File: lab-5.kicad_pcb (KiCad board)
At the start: 4 copper layers, 35 x 70 mm, 48 parts, among them J2 USB_C_Receptacle, J6 Conn_01x24_Pin, SW1 NRST, SW2 BOOT, SW3 USER, U1 LM66100DCK, U2 LM66100DCK, U3 STM32F405RGTx, U5 AP2112K-3.3, Y1 8 MHz

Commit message: add BMP280 via I2C
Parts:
- added C10: 100n, Capacitor_SMD:C_0402_1005Metric, F.Cu at (142.0, 83.7)
- added C9: 100n, Capacitor_SMD:C_0402_1005Metric, F.Cu at (142.0, 80.1)
- added U4: BMP280, Package_LGA:Bosch_LGA-8_2x2.5mm_P0.65mm_ClockwisePinNumbering, F.Cu at (142.8, 81.9)
- added U6: BMI160, Package_LGA:Bosch_LGA-14_3x2.5mm_P0.5mm, F.Cu at (142.7, 87.4)
- added U7: BMM150, Package_CSP:WLCSP-12_1.56x1.56mm_P0.4mm, F.Cu at (143.3, 92.5)
- moved R11 17.1 mm to (148.2, 88.6), turned to -90 degrees
- moved R12 16.5 mm to (148.1, 85.6)
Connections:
- J6 pad 4: /I2C1_SDA -> unconnected-(J6-Pin_4-Pad4)
- J6 pad 5: /I2C1_SCL -> unconnected-(J6-Pin_5-Pad5)
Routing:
- net GND: track 41.1 -> 44.8 mm, vias 35 -> 38
- net +3.3V: track 24.7 -> 28.3 mm, vias 19 -> 22
- net /I2C1_SDA: track 22.1 -> 23.1 mm, vias 0 -> 2
- net /I2C1_SCL: track 22.0 -> 22.7 mm, vias 0 -> 2

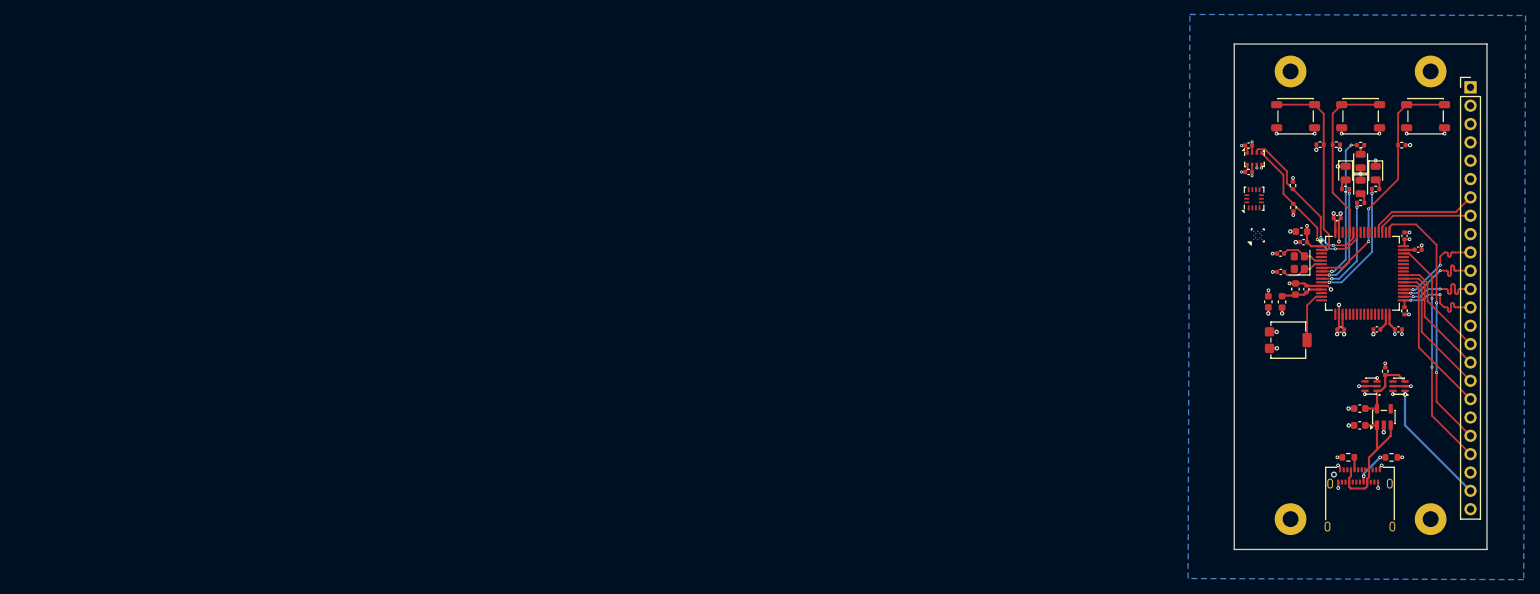
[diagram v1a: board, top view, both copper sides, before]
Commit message: added the BMI160 and logo, full board refactoring
Signed-off-by: Yehor Bilous <bilous801@gmail.com>
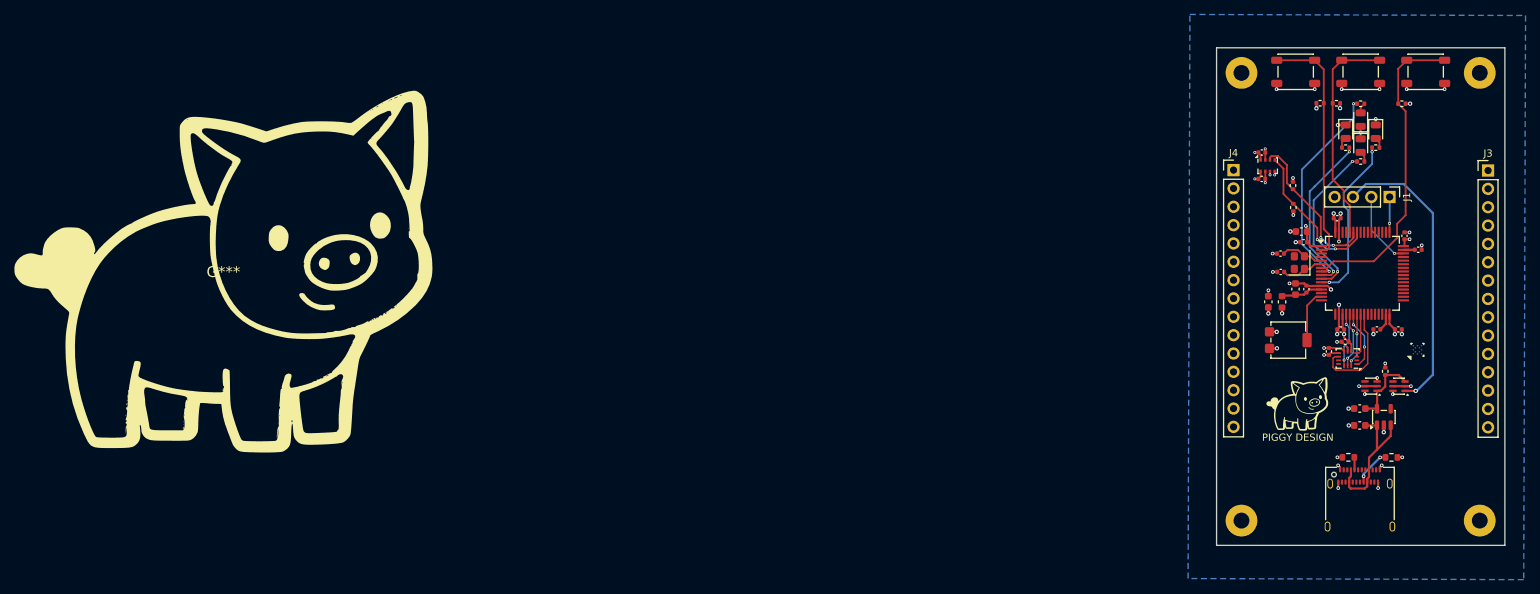
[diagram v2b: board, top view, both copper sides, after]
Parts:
- removed J6: Conn_01x24_Pin, Connector_PinHeader_2.54mm:PinHeader_1x24_P2.54mm_Vertical
- removed R14: 4.7k, Resistor_SMD:R_0402_1005Metric
- added C17: 100n, Capacitor_SMD:C_0402_1005Metric, F.Cu at (153.1, 108.6)
- added C18: 100n, Capacitor_SMD:C_0402_1005Metric, F.Cu at (155.4, 107.2)
- added G***: LOGO, logos:logo, F.Cu at (0.00, 97.6)
- added G***: LOGO, logos:logo10x10, F.Cu at (148.7, 115.8)
- added J1: Conn_01x04_Pin, Connector_PinHeader_2.54mm:PinHeader_1x04_P2.54mm_Vertical, F.Cu at (161.5, 87.2)
- added J3: Conn_01x15_Pin, Connector_PinHeader_2.54mm:PinHeader_1x15_P2.54mm_Vertical, F.Cu at (175.2, 83.5)
- added J4: Conn_01x15_Pin, Connector_PinHeader_2.54mm:PinHeader_1x15_P2.54mm_Vertical, F.Cu at (139.9, 83.5)
- moved U7 27.2 mm to (165.4, 108.3)
- moved U6 25.6 mm to (155.7, 109.6), turned to 180 degrees
- moved H1 6.80 mm to (141.0, 70.0)
- moved H2 6.80 mm to (174.0, 70.0)
- moved H3 6.80 mm to (141.0, 132.0)
- moved H4 6.80 mm to (174.0, 132.0)
- moved SW1 6.15 mm to (166.5, 69.8)
- moved SW2 6.15 mm to (157.5, 69.8)
- moved SW3 6.15 mm to (148.5, 69.8)
- moved D1 5.73 mm to (157.5, 76.5)
- moved D3 5.73 mm to (157.5, 80.1)
- moved R10 5.73 mm to (159.6, 80.3)
- moved R4 5.73 mm to (157.5, 74.3)
- moved R5 5.73 mm to (163.2, 74.3)
- moved R6 5.73 mm to (154.2, 74.2)
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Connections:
- net /USER renamed /USER_BUTTON
- U3 pad 20: unconnected-(U3-PA4-Pad20) -> /SPI1_NSS
- U3 pad 21: unconnected-(U3-PA5-Pad21) -> /SPI1_SCK
- U3 pad 22: unconnected-(U3-PA6-Pad22) -> /SPI1_MISO
- U3 pad 23: unconnected-(U3-PA7-Pad23) -> /SPI1_MOSI
- U3 pad 24: unconnected-(U3-PC4-Pad24) -> /GPIO_EXTI4
- U3 pad 25: unconnected-(U3-PC5-Pad25) -> /GPIO_EXTI5
- U3 pad 28: unconnected-(U3-PB2-Pad28) -> /GPIO_EXTI2
- U3 pad 29: unconnected-(U3-PB10-Pad29) -> /I2C2_SCL
- U3 pad 30: unconnected-(U3-PB11-Pad30) -> /I2C2_SDA
- U3 pad 33: /SPI_NSS -> unconnected-(U3-PB12-Pad33)
- U3 pad 34: /SPI_SCK -> unconnected-(U3-PB13-Pad34)
- U3 pad 35: /SPI_MISO -> unconnected-(U3-PB14-Pad35)
- U3 pad 36: /SPI_MOSI -> unconnected-(U3-PB15-Pad36)
- U3 pad 37: /GPIOC_6 -> unconnected-(U3-PC6-Pad37)
- U3 pad 38: /GPIOC_7 -> unconnected-(U3-PC7-Pad38)
- U3 pad 39: /GPIOC_8 -> unconnected-(U3-PC8-Pad39)
- U3 pad 40: /GPIOC_9 -> unconnected-(U3-PC9-Pad40)
- U3 pad 46: /SWDIO -> /SYS_JTMS_SWDIO
- U3 pad 49: /SWCLK -> /SYS_JTMS_SWCLK
- U3 pad 51: /UART_TX -> unconnected-(U3-PC10-Pad51)
- U3 pad 52: /UART_RX -> unconnected-(U3-PC11-Pad52)
- U6 pad 1: unconnected-(U6-SDO-Pad1) -> /SPI1_MISO
- U6 pad 12: unconnected-(U6-CSB-Pad12) -> /SPI1_NSS
- U6 pad 13: unconnected-(U6-SCx-Pad13) -> /SPI1_SCK
- U6 pad 14: unconnected-(U6-SDx-Pad14) -> /SPI1_MOSI
- U6 pad 4: unconnected-(U6-INT1-Pad4) -> /GPIO_EXTI4
- U6 pad 5: unconnected-(U6-VDDIO-Pad5) -> +3.3V
- U6 pad 6: unconnected-(U6-GNDIO-Pad6) -> GND
- U6 pad 7: unconnected-(U6-GND-Pad7) -> GND
- U6 pad 8: unconnected-(U6-VDD-Pad8) -> +3.3V
- U6 pad 9: unconnected-(U6-INT2-Pad9) -> /GPIO_EXTI5
- U7 pad A3: unconnected-(U7-SCK-PadA3) -> /I2C2_SCL
- U7 pad B4: unconnected-(U7-SDI-PadB4) -> /I2C2_SDA
- U7 pad D2: unconnected-(U7-INT-PadD2) -> /GPIO_EXTI2
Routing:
- net /SWCLK: track 37.0 -> 0.00 mm, vias 2 -> 0
- net /SWDIO: track 32.1 -> 0.00 mm, vias 2 -> 0
- net +3.3V_STLINK_IN: track 17.6 -> 40.6 mm
- net /GPIOC_6: track 20.5 -> 0.00 mm
- net /GPIOC_7: track 18.6 -> 0.00 mm
- net /GPIOC_8: track 16.7 -> 0.00 mm
- net /UART_RX: track 15.3 -> 0.00 mm
- net /GPIOC_9: track 14.7 -> 0.00 mm
- net /GPIO_EXTI5: track 0.00 -> 14.5 mm
- net /SPI_NSS: track 13.9 -> 0.00 mm, vias 2 -> 0
- net /UART_TX: track 13.6 -> 0.00 mm
- net /SPI_MOSI: track 13.0 -> 0.00 mm, vias 2 -> 0
- net /SPI_MISO: track 13.0 -> 0.00 mm, vias 2 -> 0
- net /SPI_SCK: track 13.0 -> 0.00 mm, vias 2 -> 0
- net /SYS_JTMS_SWDIO: track 0.00 -> 10.4 mm, vias 0 -> 1
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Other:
- board size 35 x 70 mm -> 39.9 x 68.9 mm
- board text added: "PIGGY DESIGN"

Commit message: Added bmm150 and connected all other interfaces
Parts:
- removed the G*** at (0.00, 97.6)
- added C19: 100n, Capacitor_SMD:C_0402_1005Metric, F.Cu at (171.1, 117.4)
- added C20: 100n, Capacitor_SMD:C_0402_1005Metric, F.Cu at (166.7, 116.5)
- added R13: 4.7k, Resistor_SMD:R_0402_1005Metric, F.Cu at (169.8, 97.5)
- added R14: 4.7k, Resistor_SMD:R_0402_1005Metric, F.Cu at (169.7, 94.9)
- added R15: 4.7k, Resistor_SMD:R_0402_1005Metric, F.Cu at (142.7, 101.2)
- added R16: 4.7k, Resistor_SMD:R_0402_1005Metric, F.Cu at (142.7, 96.9)
- moved U7 9.44 mm to (168.9, 117.1), turned to 180 degrees
- moved C5 1.92 mm to (163.2, 103.7)
- moved C13 1.25 mm to (161.0, 105.5), turned to 90 degrees
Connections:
- J3 pad 1: unconnected-(J3-Pin_1-Pad1) -> +3.3V
- J3 pad 10: unconnected-(J3-Pin_10-Pad10) -> /SPI2_MISO
- J3 pad 11: unconnected-(J3-Pin_11-Pad11) -> /SPI2_SCK
- J3 pad 12: unconnected-(J3-Pin_12-Pad12) -> /SPI2_NSS
- J3 pad 13: unconnected-(J3-Pin_13-Pad13) -> GND
- J3 pad 14: unconnected-(J3-Pin_14-Pad14) -> /UART4_RX
- J3 pad 15: unconnected-(J3-Pin_15-Pad15) -> /UART4_TX
- J3 pad 2: unconnected-(J3-Pin_2-Pad2) -> GND
- J3 pad 3: unconnected-(J3-Pin_3-Pad3) -> /GPIOB_9
- J3 pad 4: unconnected-(J3-Pin_4-Pad4) -> /GPIOB_8
- J3 pad 5: unconnected-(J3-Pin_5-Pad5) -> GND
- J3 pad 6: unconnected-(J3-Pin_6-Pad6) -> /I2C2_SDA
- J3 pad 7: unconnected-(J3-Pin_7-Pad7) -> /I2C2_SCL
- J3 pad 8: unconnected-(J3-Pin_8-Pad8) -> GND
- J3 pad 9: unconnected-(J3-Pin_9-Pad9) -> /SPI2_MOSI
- J4 pad 1: unconnected-(J4-Pin_1-Pad1) -> +3.3V
- J4 pad 10: unconnected-(J4-Pin_10-Pad10) -> /SPI3_MOSI
- J4 pad 11: unconnected-(J4-Pin_11-Pad11) -> /SPI3_MISO
- J4 pad 12: unconnected-(J4-Pin_12-Pad12) -> /SPI3_SCK
- J4 pad 13: unconnected-(J4-Pin_13-Pad13) -> GND
- J4 pad 14: unconnected-(J4-Pin_14-Pad14) -> /UART5_RX
- J4 pad 15: unconnected-(J4-Pin_15-Pad15) -> /UART5_TX
- J4 pad 2: unconnected-(J4-Pin_2-Pad2) -> GND
- J4 pad 3: unconnected-(J4-Pin_3-Pad3) -> /GPIOC_7
- J4 pad 4: unconnected-(J4-Pin_4-Pad4) -> /GPIOC_6
- J4 pad 5: unconnected-(J4-Pin_5-Pad5) -> GND
- J4 pad 6: unconnected-(J4-Pin_6-Pad6) -> /I2C3_SDA
- J4 pad 7: unconnected-(J4-Pin_7-Pad7) -> /I2C3_SCL
- J4 pad 8: unconnected-(J4-Pin_8-Pad8) -> GND
- J4 pad 9: unconnected-(J4-Pin_9-Pad9) -> /SPI3_NSS
- U3 pad 33: unconnected-(U3-PB12-Pad33) -> /SPI2_NSS
- U3 pad 34: unconnected-(U3-PB13-Pad34) -> /SPI2_SCK
- U3 pad 35: unconnected-(U3-PB14-Pad35) -> /SPI2_MISO
- U3 pad 36: unconnected-(U3-PB15-Pad36) -> /SPI2_MOSI
- U3 pad 37: unconnected-(U3-PC6-Pad37) -> /GPIOC_6
- U3 pad 38: unconnected-(U3-PC7-Pad38) -> /GPIOC_7
- U3 pad 40: unconnected-(U3-PC9-Pad40) -> /I2C3_SDA
- U3 pad 41: unconnected-(U3-PA8-Pad41) -> /I2C3_SCL
- U3 pad 50: unconnected-(U3-PA15-Pad50) -> /SPI3_NSS
- U3 pad 51: unconnected-(U3-PC10-Pad51) -> /UART4_TX
- U3 pad 52: unconnected-(U3-PC11-Pad52) -> /UART4_RX
- U3 pad 53: unconnected-(U3-PC12-Pad53) -> /UART5_TX
- U3 pad 54: unconnected-(U3-PD2-Pad54) -> /UART5_RX
- U3 pad 55: unconnected-(U3-PB3-Pad55) -> /SPI3_SCK
- U3 pad 56: unconnected-(U3-PB4-Pad56) -> /SPI3_MISO
- U3 pad 57: unconnected-(U3-PB5-Pad57) -> /SPI3_MOSI
- U3 pad 61: unconnected-(U3-PB8-Pad61) -> /GPIOB_8
- U3 pad 62: unconnected-(U3-PB9-Pad62) -> /GPIOB_9
- U7 pad A1: unconnected-(U7-PS-PadA1) -> +3.3V
- U7 pad A3: /I2C2_SCL -> /I2C1_SCL
- U7 pad A5: unconnected-(U7-CSB-PadA5) -> +3.3V
- U7 pad B2: unconnected-(U7-VDDIO-PadB2) -> +3.3V
- U7 pad B4: /I2C2_SDA -> /I2C1_SDA
- U7 pad C1: unconnected-(U7-SDO-PadC1) -> +3.3V
- U7 pad C5: Net-(U7-GND-PadC5) -> GND
- U7 pad D2: /GPIO_EXTI2 -> unconnected-(U7-INT-PadD2)
- U7 pad D4: unconnected-(U7-DRDY-PadD4) -> /GPIO_EXTI2
- U7 pad E1: Net-(U7-GND-PadC5) -> GND
- U7 pad E3: Net-(U7-GND-PadC5) -> GND
- U7 pad E5: unconnected-(U7-VDD-PadE5) -> +3.3V
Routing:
- net /I2C1_SDA: track 21.4 -> 59.7 mm, vias 2 -> 4
- net /GPIOB_9: track 0.00 -> 36.0 mm, vias 0 -> 1
- net /SPI3_SCK: track 0.00 -> 35.9 mm, vias 0 -> 1
- net /UART5_TX: track 0.00 -> 35.7 mm, vias 0 -> 2
- net /SPI3_MOSI: track 0.00 -> 35.7 mm, vias 0 -> 1
- net /SPI3_MISO: track 0.00 -> 35.7 mm, vias 0 -> 1
- net /UART5_RX: track 0.00 -> 35.7 mm, vias 0 -> 2
- net /SPI3_NSS: track 0.00 -> 35.7 mm, vias 0 -> 1
- net /UART4_TX: track 0.00 -> 35.5 mm, vias 0 -> 2
- net /I2C1_SCL: track 21.0 -> 55.4 mm, vias 2 -> 4
- net /UART4_RX: track 0.00 -> 31.8 mm, vias 0 -> 2
- net /I2C3_SDA: track 0.00 -> 30.5 mm, vias 0 -> 4
- net /I2C3_SCL: track 0.00 -> 29.4 mm, vias 0 -> 4
- net /GPIOB_8: track 0.00 -> 28.9 mm, vias 0 -> 2
- net /GPIOC_7: track 0.00 -> 28.3 mm, vias 0 -> 3
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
